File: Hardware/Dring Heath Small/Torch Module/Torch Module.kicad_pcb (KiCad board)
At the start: 2 copper layers, 91.6 x 79.4 mm, 45 parts, among them J1 Torch, J10 Module conn, J11 Conn_01x18_Male, J2 Module3, J3 Conn_01x18_Male, J4 Limit, J6 Motor, J7 Module1, J8 Torch, J9 2.54 pin, K1 G6E, Q1 IRLML2402, Q2 IRLML2402, Q3 IRLML2402, Q4 IRLML2402, Q5 IRLML2402, U1 ULN2002

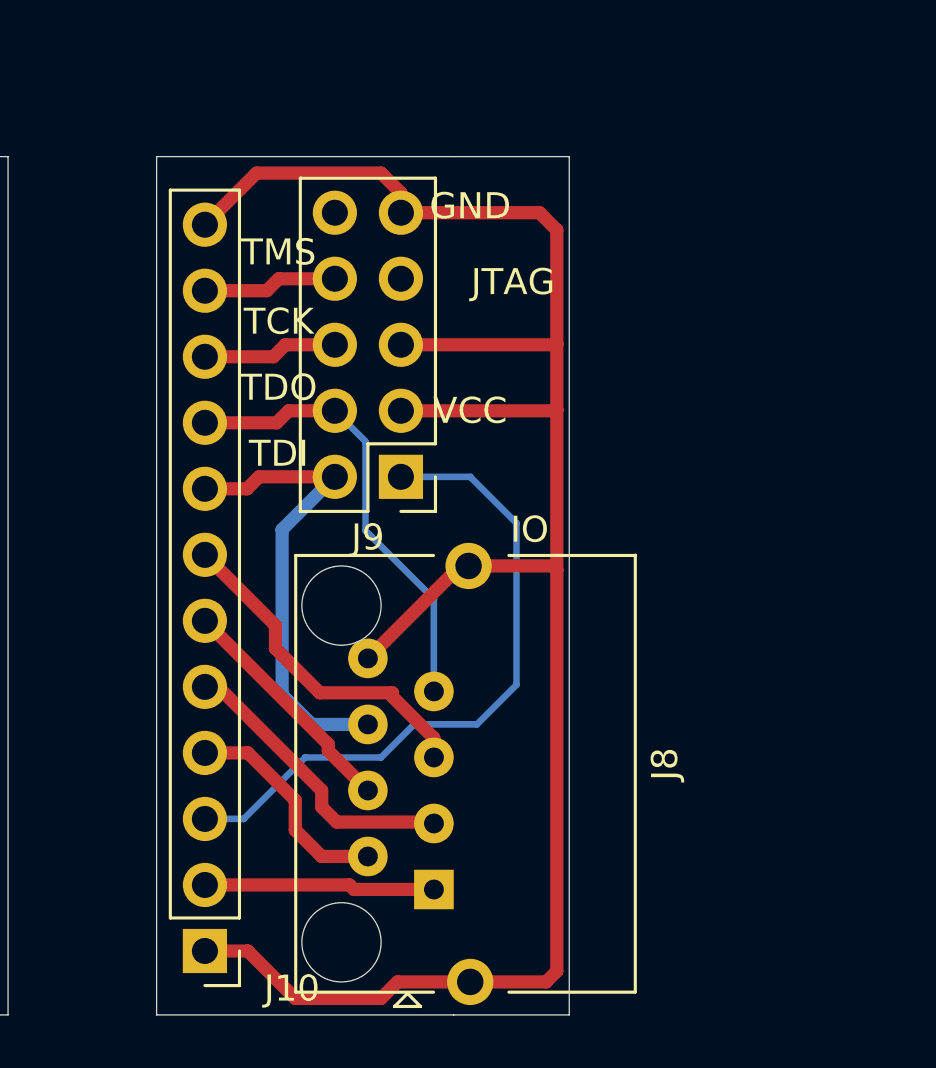
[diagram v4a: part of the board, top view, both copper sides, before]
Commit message: put protection resistors on JTAG module
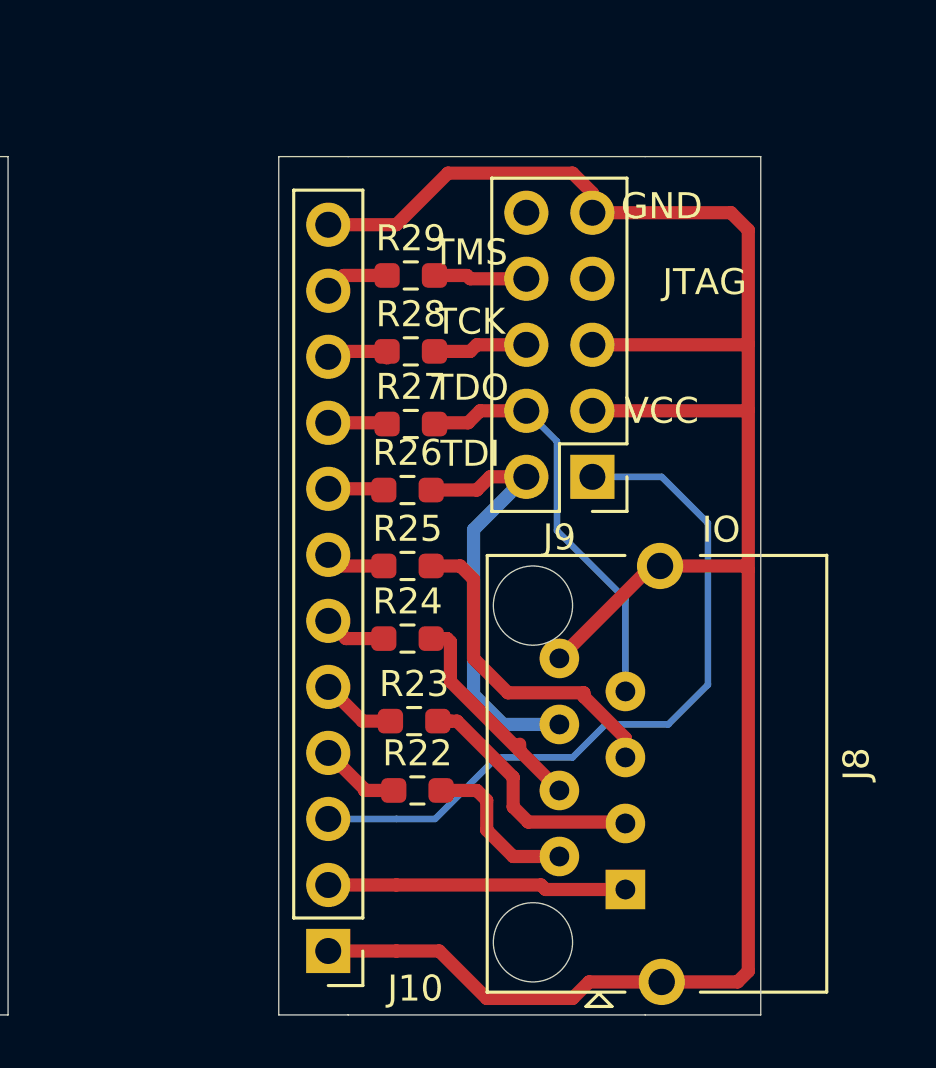
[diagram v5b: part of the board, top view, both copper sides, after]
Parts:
- added R22: 200, Resistor_SMD:R_0603_1608Metric_Pad0.98x0.95mm_HandSolder, F.Cu at (183.4, 123.4)
- added R23: 200, Resistor_SMD:R_0603_1608Metric_Pad0.98x0.95mm_HandSolder, F.Cu at (183.3, 120.8)
- added R24: 200, Resistor_SMD:R_0603_1608Metric_Pad0.98x0.95mm_HandSolder, F.Cu at (183.0, 117.6)
- added R25: 200, Resistor_SMD:R_0603_1608Metric_Pad0.98x0.95mm_HandSolder, F.Cu at (183.0, 114.8)
- added R26: 200, Resistor_SMD:R_0603_1608Metric_Pad0.98x0.95mm_HandSolder, F.Cu at (183.0, 111.9)
- added R27: 200, Resistor_SMD:R_0603_1608Metric_Pad0.98x0.95mm_HandSolder, F.Cu at (183.1, 109.3)
- added R28: 200, Resistor_SMD:R_0603_1608Metric_Pad0.98x0.95mm_HandSolder, F.Cu at (183.1, 106.6)
- added R29: 200, Resistor_SMD:R_0603_1608Metric_Pad0.98x0.95mm_HandSolder, F.Cu at (183.1, 103.6)
- moved J9 7.37 mm to (190.1, 111.4)
- moved J8 7.37 mm to (190.4, 127.3)
- moved J10 4.75 mm to (180.0, 129.6)
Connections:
- J8 pad 2: Net-(J10-Pad4) -> Net-(J8-Pad2)
- J8 pad 3: Net-(J10-Pad5) -> Net-(J8-Pad3)
- J8 pad 4: Net-(J10-Pad6) -> Net-(J8-Pad4)
- J8 pad 5: Net-(J10-Pad7) -> Net-(J8-Pad5)
- J8 pad 6: Net-(J10-Pad8) -> Net-(J8-Pad6)
- J8 pad 7: Net-(J10-Pad9) -> Net-(J8-Pad7)
- J9 pad 2: Net-(J10-Pad8) -> Net-(J8-Pad6)
- J9 pad 4: Net-(J10-Pad9) -> Net-(J8-Pad7)
- J9 pad 6: Net-(J10-Pad10) -> Net-(J9-Pad6)
- J9 pad 8: Net-(J10-Pad11) -> Net-(J9-Pad8)
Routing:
- net Net-(J8-Pad6): track 0.00 -> 16.9 mm
- net Net-(J8-Pad7): track 0.00 -> 16.2 mm
- net Net-(J10-Pad8): track 18.3 -> 2.15 mm
- net Net-(J10-Pad9): track 17.6 -> 2.28 mm
- net Net-(J8-Pad5): track 0.00 -> 12.8 mm
- net Net-(J10-Pad7): track 13.1 -> 2.56 mm
- net Net-(J8-Pad3): track 0.00 -> 10.0 mm
- net Net-(J8-Pad4): track 0.00 -> 8.50 mm
- net Net-(J10-Pad5): track 11.4 -> 2.94 mm
- net Net-(J10-Pad6): track 9.12 -> 2.66 mm
- net Net-(J8-Pad2): track 0.00 -> 6.27 mm
- net Net-(J10-Pad4): track 8.59 -> 3.14 mm
- net Net-(J10-Pad1): track 79.8 -> 85.0 mm
- net Net-(J9-Pad6): track 0.00 -> 3.70 mm
- net Net-(J9-Pad8): track 0.00 -> 3.65 mm
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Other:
- board size 91.6 x 79.4 mm -> 98.9 x 79.4 mm

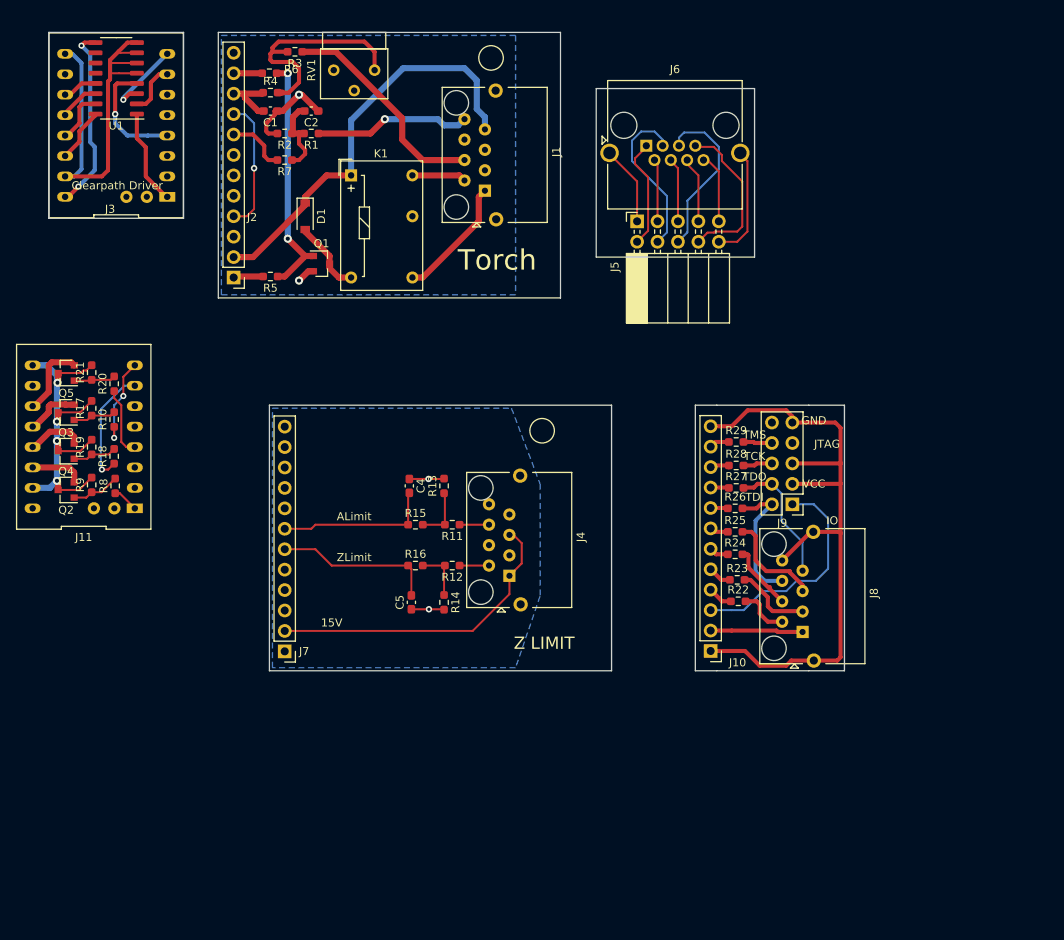
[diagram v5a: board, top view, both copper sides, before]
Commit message: Tidied module boards
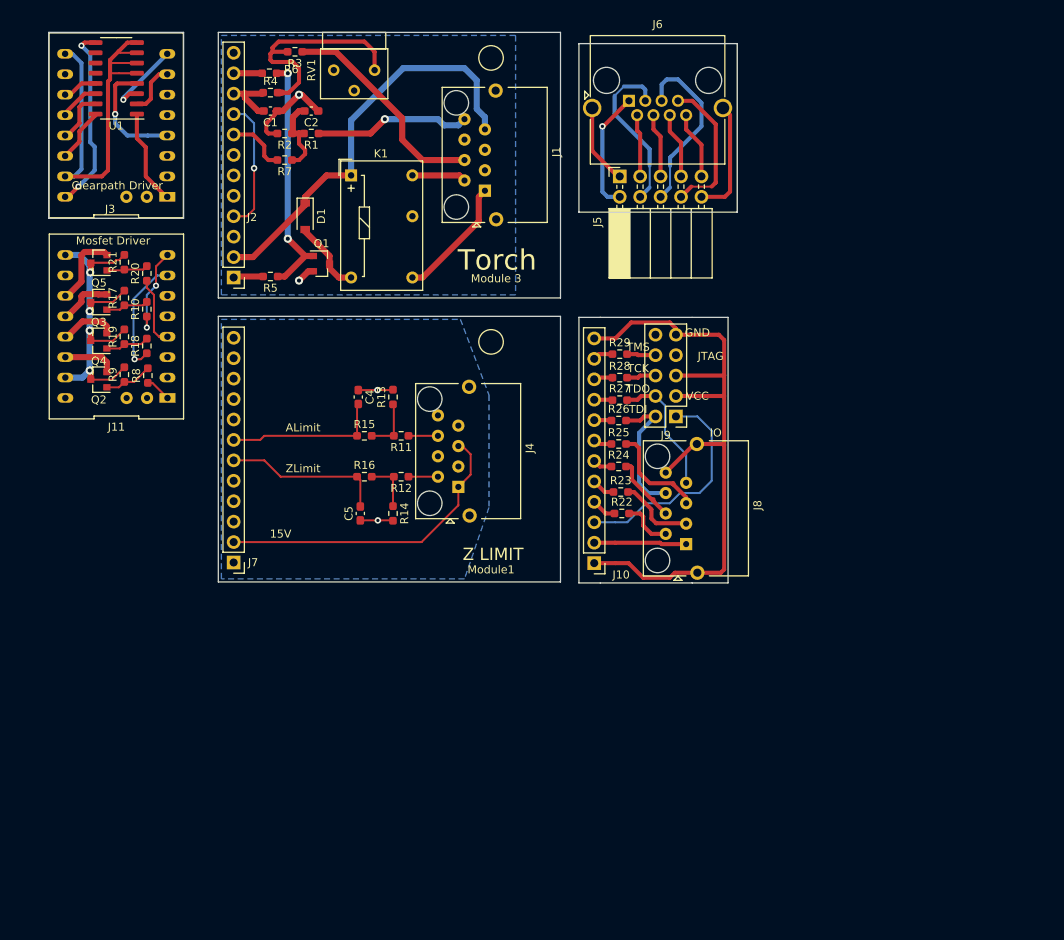
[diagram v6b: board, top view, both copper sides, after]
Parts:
- moved J10 18.1 mm to (165.5, 118.7)
- moved J9 18.1 mm to (175.6, 100.5)
- moved R25 18.1 mm to (168.5, 103.9)
- moved R22 18.1 mm to (168.9, 112.5)
- moved R23 18.1 mm to (168.8, 109.9)
- moved R24 18.1 mm to (168.5, 106.7)
- moved R26 18.1 mm to (168.5, 101.0)
- moved J8 18.1 mm to (175.9, 116.3)
- moved R29 18.1 mm to (168.7, 92.7)
- moved R27 18.1 mm to (168.7, 98.4)
- moved R28 18.1 mm to (168.7, 95.6)
- moved J11 14.3 mm to (106.1, 89.3)
- moved R17 14.3 mm to (107.1, 85.7)
- moved Q4 14.3 mm to (103.9, 91.1)
- moved R8 14.3 mm to (110.0, 95.4)
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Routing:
- net Net-(J5-Pad6): track 21.0 -> 23.5 mm
- net Net-(J5-Pad4): track 20.5 -> 22.5 mm
- net Net-(J5-Pad2): track 13.6 -> 15.2 mm, vias 0 -> 1
- net Net-(J5-Pad8): track 19.9 -> 18.6 mm
- net Net-(J5-Pad3): track 7.62 -> 8.28 mm
- net Net-(J5-Pad10): track 14.1 -> 14.6 mm
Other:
- board size 98.9 x 79.4 mm -> 85.6 x 68.5 mm
- board text added: "Module 3"
- board text added: "Module1"
- board text added: "Mosfet Driver"

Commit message: fixed voltage divider for THC
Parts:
- C1: value 22nf -> 100nf
- R3: value 1k -> 3.3K
- R7: value 10k -> 200

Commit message: routed a/d board
put simulation on excel bom
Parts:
- added C3: 100nf, Capacitor_SMD:C_0603_1608Metric_Pad1.08x0.95mm_HandSolder, F.Cu at (216.7, 109.5)
- added C6: 1uf, Capacitor_SMD:C_0603_1608Metric_Pad1.08x0.95mm_HandSolder, F.Cu at (208.9, 109.3)
- added C7: 100nf, Capacitor_SMD:C_0603_1608Metric_Pad1.08x0.95mm_HandSolder, F.Cu at (214.3, 99.9)
- added C8: 1uf, Capacitor_SMD:C_0603_1608Metric_Pad1.08x0.95mm_HandSolder, F.Cu at (209.1, 115.8)
- added D2: D_Schottky_Small, Diode_SMD:D_0805_2012Metric_Pad1.15x1.40mm_HandSolder, F.Cu at (215.1, 103.2)
- added D3: D_Schottky_Small, Diode_SMD:D_0805_2012Metric_Pad1.15x1.40mm_HandSolder, F.Cu at (218.6, 103.3)
- added FB1: BLM18HE152SN1D, Resistor_SMD:R_0603_1608Metric_Pad0.98x0.95mm_HandSolder, F.Cu at (210.1, 118.9)
- added FB2: ~, Resistor_SMD:R_0603_1608Metric_Pad0.98x0.95mm_HandSolder, F.Cu at (210.1, 113.0)
- added J12: Conn_01x02_Male, Connector_PinHeader_2.54mm:PinHeader_1x02_P2.54mm_Vertical, F.Cu at (218.0, 116.3)
- added J13: ~, Connector_PinHeader_2.54mm:PinHeader_2x02_P2.54mm_Vertical, F.Cu at (146.0, 57.0)
- added J14: Conn_01x02_Male, Connector_PinHeader_2.54mm:PinHeader_1x02_P2.54mm_Vertical, F.Cu at (128.0, 55.0)
- added J15: Module conn, Connector_PinHeader_2.54mm:PinHeader_1x12_P2.54mm_Vertical, F.Cu at (205.3, 117.9)
- added R30: 1k, Resistor_SMD:R_0603_1608Metric_Pad0.98x0.95mm_HandSolder, F.Cu at (218.0, 112.4)
- added R31: 1k, Resistor_SMD:R_0603_1608Metric_Pad0.98x0.95mm_HandSolder, F.Cu at (215.5, 112.4)
- added R32: 1k, Resistor_SMD:R_0603_1608Metric_Pad0.98x0.95mm_HandSolder, F.Cu at (219.4, 108.6)
- added R33: 1k, Resistor_SMD:R_0603_1608Metric_Pad0.98x0.95mm_HandSolder, F.Cu at (214.1, 108.6)
- added R34: 2.4K, Resistor_SMD:R_0603_1608Metric_Pad0.98x0.95mm_HandSolder, F.Cu at (220.3, 91.0)
- added R35: 2.4K, Resistor_SMD:R_0603_1608Metric_Pad0.98x0.95mm_HandSolder, F.Cu at (212.9, 91.0)
- added R36: 2.4K, Resistor_SMD:R_0603_1608Metric_Pad0.98x0.95mm_HandSolder, F.Cu at (209.6, 90.9)
- added R37: 2.4K, Resistor_SMD:R_0603_1608Metric_Pad0.98x0.95mm_HandSolder, F.Cu at (216.3, 91.0)
- added U2: NCV8114ASN150T1G, Package_TO_SOT_SMD:TSOT-23-5, F.Cu at (209.6, 104.9)
- added U3: ADS1115IDGS, Package_SO:TSSOP-10_3x3mm_P0.5mm, F.Cu at (214.6, 94.8)
- moved R3 19.1 mm to (144.0, 66.0)
- moved R4 5.26 mm to (130.0, 58.0), turned to 270 degrees
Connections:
- J1 pad 3: Net-(C1-Pad1) -> Net-(J1-Pad3)
- J2 pad 10: Net-(C1-Pad2) -> Net-(J14-Pad2)
- R3 pad 1: Net-(J1-Pad4) -> Net-(J13-Pad2)
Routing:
- net Net-(C7-Pad1): track 0.00 -> 70.6 mm
- net Net-(C8-Pad2): track 0.00 -> 35.7 mm
- net Net-(J1-Pad3): track 0.00 -> 27.7 mm
- net Net-(C3-Pad1): track 0.00 -> 26.7 mm, vias 0 -> 2
- net Net-(C3-Pad2): track 0.00 -> 26.2 mm, vias 0 -> 2
- net Net-(C6-Pad1): track 0.00 -> 24.3 mm, vias 0 -> 3
- net Net-(J15-Pad9): track 0.00 -> 21.9 mm, vias 0 -> 2
- net Net-(C6-Pad2): track 0.00 -> 17.6 mm, vias 0 -> 5
- net Net-(J1-Pad4): track 27.3 -> 13.0 mm
- net Net-(J15-Pad10): track 0.00 -> 12.0 mm, vias 0 -> 1
- net Net-(J15-Pad11): track 0.00 -> 11.7 mm
- net Net-(J13-Pad2): track 0.00 -> 11.1 mm
- net Net-(J14-Pad2): track 0.00 -> 8.77 mm
- net Net-(R34-Pad1): track 0.00 -> 7.29 mm
- net Net-(C8-Pad1): track 0.00 -> 6.51 mm
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- added copper zone on B.Cu, net Net-(C6-Pad2)
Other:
- board size 85.6 x 68.5 mm -> 124 x 68.5 mm
- board text added: "A/D"
